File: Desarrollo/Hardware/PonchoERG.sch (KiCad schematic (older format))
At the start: 1 part

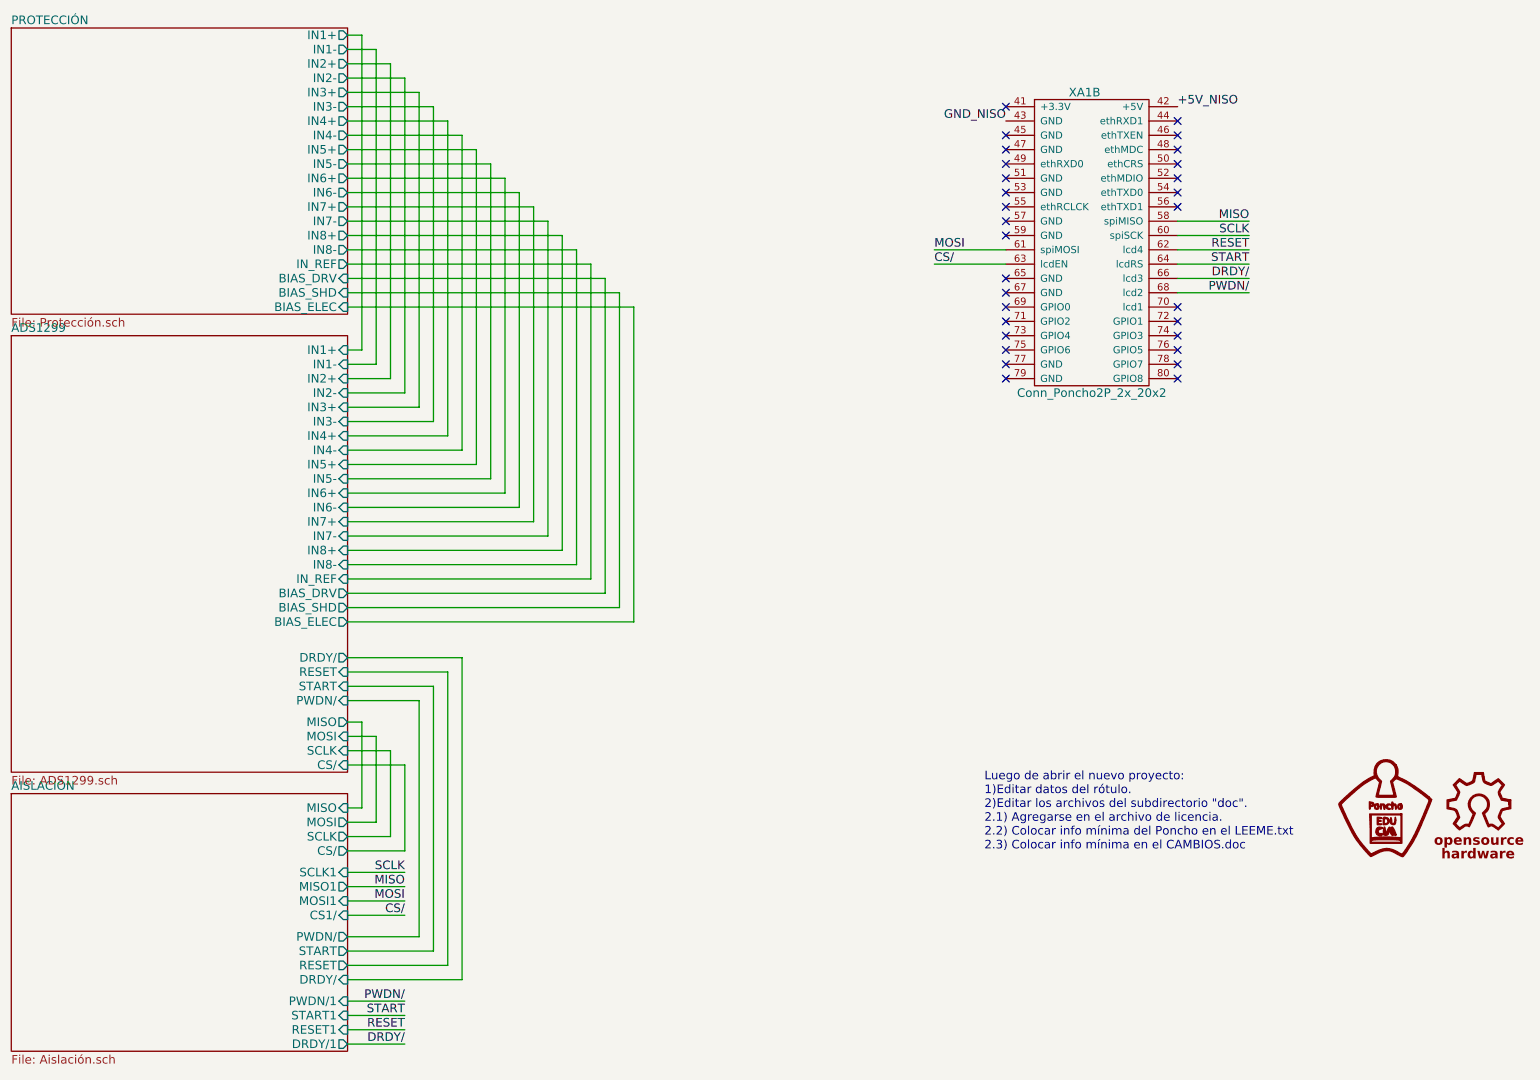
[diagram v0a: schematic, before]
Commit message: Revert "Finalización de primer ruteo estimado. Revisión de cantidad de v"
This reverts commit b379d941abb4cafe5355ba8bbe61a2a3831aeef6.
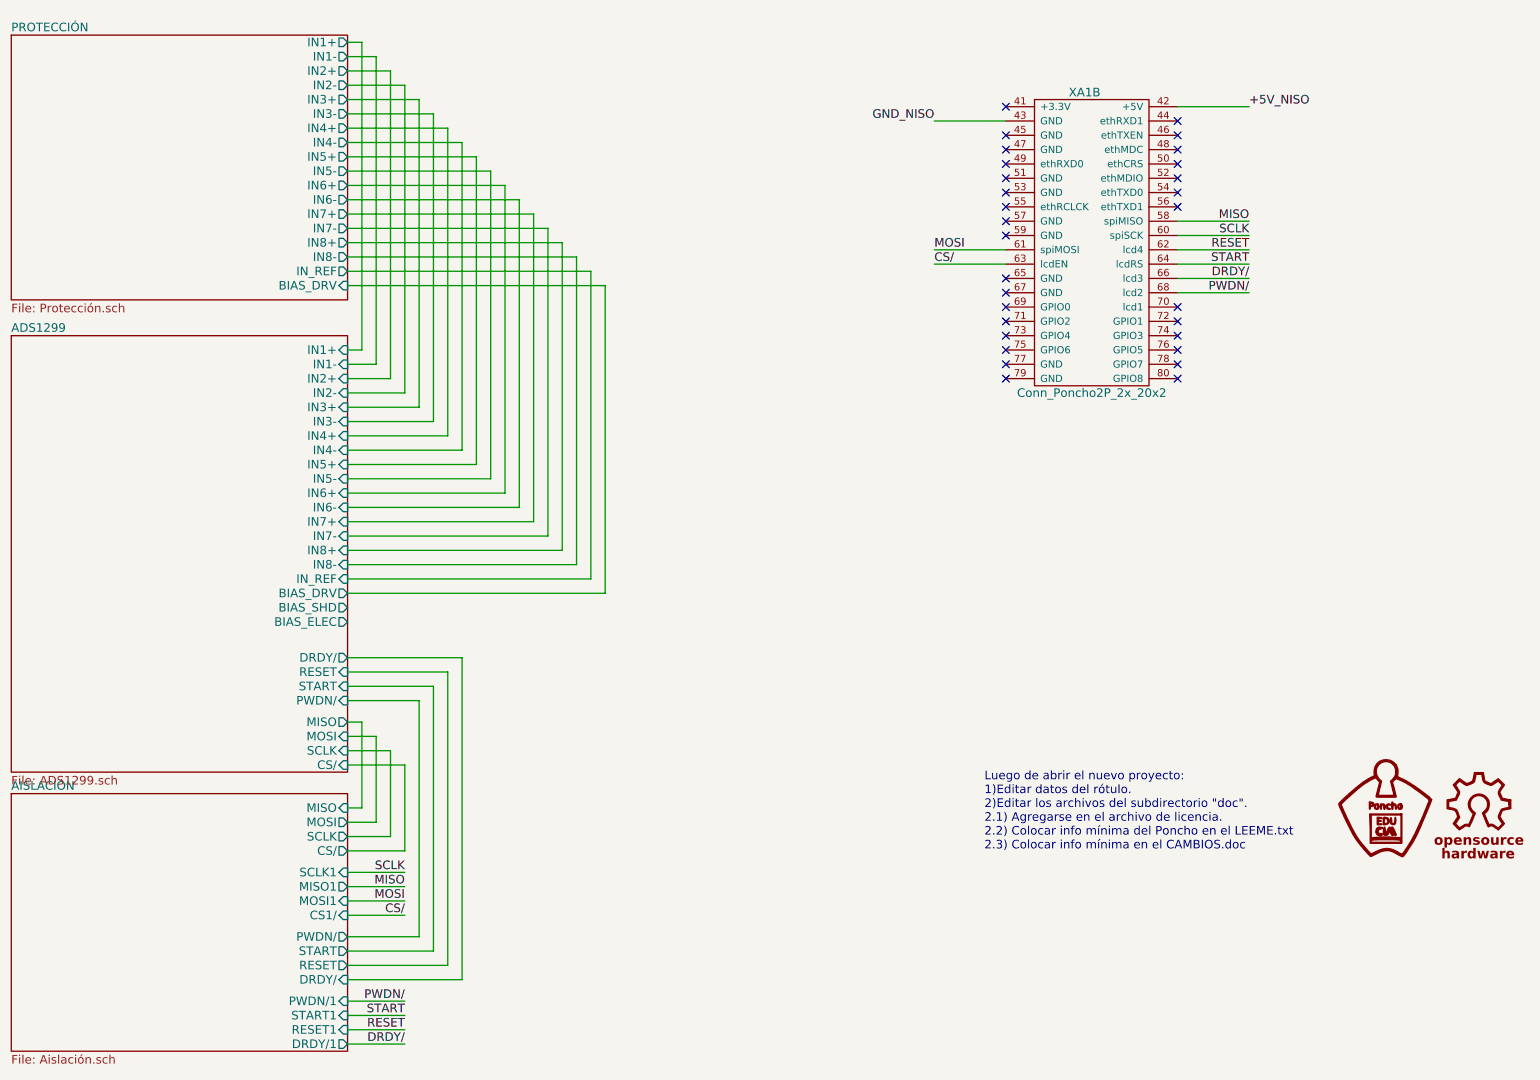
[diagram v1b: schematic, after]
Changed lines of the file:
@@
 Date "lun 05 oct 2015"
 Rev "1.0"
-Comp "Bruno Javier Cesario"
+Comp "Proyecto CIAA - COMPUTADORA INDUSTRIAL ABIERTA ARGENTINA"
 Comment1 "https://github.com/ciaa/Ponchos/tree/master/modelos/doc"
 Comment2 "Autores y Licencia del template (Diego Brengi - UNLaM)"
@@
 Luego de abrir el nuevo proyecto:\n1)Editar datos del rótulo.\n2)Editar los archivos del subdirectorio "doc".\n2.1) Agregarse en el archivo de licencia.\n2.2) Colocar info mínima del Poncho en el LEEME.txt\n2.3) Colocar info mínima en el CAMBIOS.doc
 $Sheet
-S 550  550  2350 2000
+S 550  600  2350 1850
 U 57BDBDC8
 F0 "PROTECCIÓN" 60
 F1 "Protección.sch" 60
-F2 "IN2-" O R 2900 900 60
-F3 "IN3+" O R 2900 1000 60
-F4 "IN3-" O R 2900 1100 60
-F5 "IN4+" O R 2900 1200 60
-F6 "IN4-" O R 2900 1300 60
-F7 "IN5+" O R 2900 1400 60
-F8 "IN5-" O R 2900 1500 60
-F9 "IN6+" O R 2900 1600 60
-F10 "IN6-" O R 2900 1700 60
-F11 "IN7+" O R 2900 1800 60
-F12 "IN1+" O R 2900 600 60
-F13 "IN1-" O R 2900 700 60
-F14 "IN2+" O R 2900 800 60
-F15 "IN7-" O R 2900 1900 60
-F16 "IN8+" O R 2900 2000 60
-F17 "IN8-" O R 2900 2100 60
-F18 "IN_REF" O R 2900 2200 60
-F19 "BIAS_DRV" I R 2900 2300 60
-F20 "BIAS_SHD" I R 2900 2400 60
-F21 "BIAS_ELEC" I R 2900 2500 60
+F2 "IN2-" O R 2900 950 60
+F3 "IN3+" O R 2900 1050 60
+F4 "IN3-" O R 2900 1150 60
+F5 "IN4+" O R 2900 1250 60
+F6 "IN4-" O R 2900 1350 60
+F7 "IN5+" O R 2900 1450 60
+F8 "IN5-" O R 2900 1550 60
+F9 "IN6+" O R 2900 1650 60
+F10 "IN6-" O R 2900 1750 60
+F11 "IN7+" O R 2900 1850 60
+F12 "IN1+" O R 2900 650 60
+F13 "IN1-" O R 2900 750 60
+F14 "IN2+" O R 2900 850 60
+F15 "IN7-" O R 2900 1950 60
+F16 "IN8+" O R 2900 2050 60
+F17 "IN8-" O R 2900 2150 60
+F18 "IN_REF" O R 2900 2250 60
+F19 "BIAS_DRV" I R 2900 2350 60
 $EndSheet
 $Sheet
@@
 $EndSheet
 Wire Wire Line
-	3000 600  3000 2800
+	2900 650  3000 650
+Wire Wire Line
+	3000 650  3000 2800
 Wire Wire Line
 	3000 2800 2900 2800
 Wire Wire Line
-	3100 700  3100 2900
+	2900 750  3100 750
+Wire Wire Line
+	3100 750  3100 2900
 Wire Wire Line
 	3100 2900 2900 2900
 Wire Wire Line
-	3200 3000 2900 3000
-Wire Wire Line
-	3200 800  3200 3000
-Wire Wire Line
-	3300 900  3300 3100
+	2900 3000 3200 3000
+Wire Wire Line
+	3200 3000 3200 850
+Wire Wire Line
+	3200 850  2900 850
+Wire Wire Line
+	2900 950  3300 950
+Wire Wire Line
+	3300 950  3300 3100
 Wire Wire Line
 	3300 3100 2900 3100
 Wire Wire Line
-	3400 1000 3400 3200
+	2900 1050 3400 1050
+Wire Wire Line
+	3400 1050 3400 3200
 Wire Wire Line
 	3400 3200 2900 3200
 Wire Wire Line
-	3500 1100 3500 3300
+	2900 1150 3500 1150
+Wire Wire Line
+	3500 1150 3500 3300
 Wire Wire Line
 	3500 3300 2900 3300
 Wire Wire Line
-	3600 3400 2900 3400
-Wire Wire Line
-	3600 1200 3600 3400
-Wire Wire Line
-	3700 1300 3700 3500
+	2900 3400 3600 3400
+Wire Wire Line
+	3600 3400 3600 1250
+Wire Wire Line
+	3600 1250 2900 1250
+Wire Wire Line
+	2900 1350 3700 1350
+Wire Wire Line
+	3700 1350 3700 3500
 Wire Wire Line
 	3700 3500 2900 3500
 Wire Wire Line
-	3800 3600 2900 3600
-Wire Wire Line
-	3800 1400 3800 3600
-Wire Wire Line
-	3900 1500 3900 3700
+	2900 3600 3800 3600
+Wire Wire Line
+	3800 3600 3800 1450
+Wire Wire Line
+	3800 1450 2900 1450
+Wire Wire Line
+	2900 1550 3900 1550
+Wire Wire Line
+	3900 1550 3900 3700
 Wire Wire Line
 	3900 3700 2900 3700
 Wire Wire Line
-	4000 3800 2900 3800
-Wire Wire Line
-	4000 1600 4000 3800
-Wire Wire Line
-	4100 1700 4100 3900
+	2900 3800 4000 3800
+Wire Wire Line
+	4000 3800 4000 1650
+Wire Wire Line
+	4000 1650 2900 1650
+Wire Wire Line
+	2900 1750 4100 1750
+Wire Wire Line
+	4100 1750 4100 3900
 Wire Wire Line
 	4100 3900 2900 3900
 Wire Wire Line
-	4200 1800 4200 4000
+	2900 1850 4200 1850
+Wire Wire Line
+	4200 1850 4200 4000
 Wire Wire Line
 	4200 4000 2900 4000
 Wire Wire Line
-	4300 1900 4300 4100
+	2900 1950 4300 1950
+Wire Wire Line
+	4300 1950 4300 4100
 Wire Wire Line
 	4300 4100 2900 4100
 Wire Wire Line
-	4400 4200 2900 4200
-Wire Wire Line
-	4400 2000 4400 4200
-Wire Wire Line
-	4500 4300 2900 4300
-Wire Wire Line
-	4500 2100 4500 4300
+	2900 4200 4400 4200
+Wire Wire Line
+	4400 4200 4400 2050
+Wire Wire Line
+	4400 2050 2900 2050
+Wire Wire Line
+	2900 4300 4500 4300
+Wire Wire Line
+	4500 4300 4500 2150
+Wire Wire Line
+	4500 2150 2900 2150
 Wire Wire Line
 	3000 6000 2900 6000
@@
 	2900 6300 3300 6300
 Wire Wire Line
-	4700 2300 4700 4500
+	2900 2350 4700 2350
+Wire Wire Line
+	4700 2350 4700 4500
 Wire Wire Line
 	4700 4500 2900 4500
 Wire Wire Line
-	4600 2200 4600 4400
+	2900 2250 4600 2250
+Wire Wire Line
+	4600 2250 4600 4400
 Wire Wire Line
 	4600 4400 2900 4400
@@
 	1    0    0    -1
 $EndComp
-Text Label 8700 1100 0    60   ~ 0
+Wire Wire Line
+	8700 1100 9200 1100
+Wire Wire Line
+	7500 1200 7000 1200
+Text Label 9200 1100 0    60   ~ 0
 +5V_NISO
-Text Label 7500 1200 2    60   ~ 0
+Text Label 7000 1200 2    60   ~ 0
 GND_NISO
 Wire Wire Line
@@
 Wire Wire Line
 	3700 4950 2900 4950
-Wire Wire Line
-	2900 600  3000 600
-Wire Wire Line
-	2900 700  3100 700
-Wire Wire Line
-	2900 800  3200 800
-Wire Wire Line
-	2900 900  3300 900
-Wire Wire Line
-	2900 1000 3400 1000
-Wire Wire Line
-	2900 1100 3500 1100
-Wire Wire Line
-	2900 1200 3600 1200
-Wire Wire Line
-	2900 1300 3700 1300
-Wire Wire Line
-	2900 1400 3800 1400
-Wire Wire Line
-	2900 1500 3900 1500
-Wire Wire Line
-	2900 1600 4000 1600
-Wire Wire Line
-	4100 1700 2900 1700
-Wire Wire Line
-	2900 1800 4200 1800
-Wire Wire Line
-	2900 1900 4300 1900
-Wire Wire Line
-	2900 2000 4400 2000
-Wire Wire Line
-	2900 2100 4500 2100
-Wire Wire Line
-	2900 2200 4600 2200
-Wire Wire Line
-	2900 2300 4700 2300
-Wire Wire Line
-	2900 4600 4800 4600
-Wire Wire Line
-	4800 4600 4800 2400
-Wire Wire Line
-	4800 2400 2900 2400
-Wire Wire Line
-	2900 2500 4900 2500
-Wire Wire Line
-	4900 2500 4900 4700
-Wire Wire Line
-	4900 4700 2900 4700
 $EndSCHEMATC

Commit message: Finalización de primer ruteo estimado. Revisión de cantidad de v
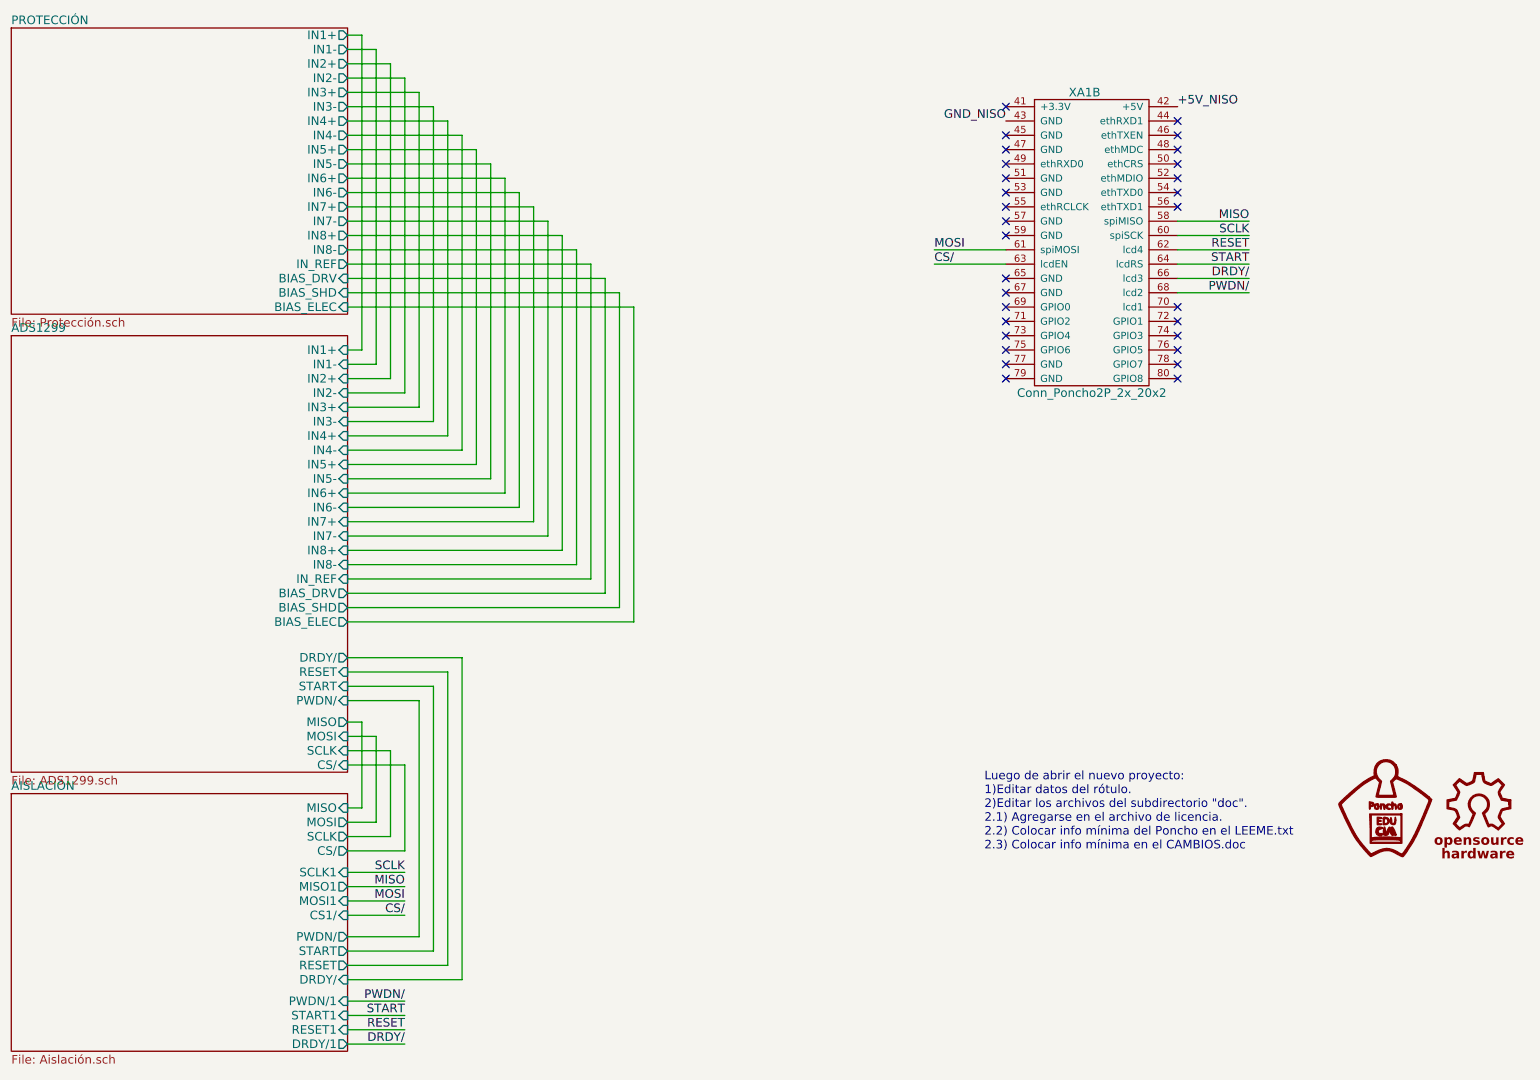
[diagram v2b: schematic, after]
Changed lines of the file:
@@
 Date "lun 05 oct 2015"
 Rev "1.0"
-Comp "Proyecto CIAA - COMPUTADORA INDUSTRIAL ABIERTA ARGENTINA"
+Comp "Bruno Javier Cesario"
 Comment1 "https://github.com/ciaa/Ponchos/tree/master/modelos/doc"
 Comment2 "Autores y Licencia del template (Diego Brengi - UNLaM)"
@@
 Luego de abrir el nuevo proyecto:\n1)Editar datos del rótulo.\n2)Editar los archivos del subdirectorio "doc".\n2.1) Agregarse en el archivo de licencia.\n2.2) Colocar info mínima del Poncho en el LEEME.txt\n2.3) Colocar info mínima en el CAMBIOS.doc
 $Sheet
-S 550  600  2350 1850
+S 550  550  2350 2000
 U 57BDBDC8
 F0 "PROTECCIÓN" 60
 F1 "Protección.sch" 60
-F2 "IN2-" O R 2900 950 60
-F3 "IN3+" O R 2900 1050 60
-F4 "IN3-" O R 2900 1150 60
-F5 "IN4+" O R 2900 1250 60
-F6 "IN4-" O R 2900 1350 60
-F7 "IN5+" O R 2900 1450 60
-F8 "IN5-" O R 2900 1550 60
-F9 "IN6+" O R 2900 1650 60
-F10 "IN6-" O R 2900 1750 60
-F11 "IN7+" O R 2900 1850 60
-F12 "IN1+" O R 2900 650 60
-F13 "IN1-" O R 2900 750 60
-F14 "IN2+" O R 2900 850 60
-F15 "IN7-" O R 2900 1950 60
-F16 "IN8+" O R 2900 2050 60
-F17 "IN8-" O R 2900 2150 60
-F18 "IN_REF" O R 2900 2250 60
-F19 "BIAS_DRV" I R 2900 2350 60
+F2 "IN2-" O R 2900 900 60
+F3 "IN3+" O R 2900 1000 60
+F4 "IN3-" O R 2900 1100 60
+F5 "IN4+" O R 2900 1200 60
+F6 "IN4-" O R 2900 1300 60
+F7 "IN5+" O R 2900 1400 60
+F8 "IN5-" O R 2900 1500 60
+F9 "IN6+" O R 2900 1600 60
+F10 "IN6-" O R 2900 1700 60
+F11 "IN7+" O R 2900 1800 60
+F12 "IN1+" O R 2900 600 60
+F13 "IN1-" O R 2900 700 60
+F14 "IN2+" O R 2900 800 60
+F15 "IN7-" O R 2900 1900 60
+F16 "IN8+" O R 2900 2000 60
+F17 "IN8-" O R 2900 2100 60
+F18 "IN_REF" O R 2900 2200 60
+F19 "BIAS_DRV" I R 2900 2300 60
+F20 "BIAS_SHD" I R 2900 2400 60
+F21 "BIAS_ELEC" I R 2900 2500 60
 $EndSheet
 $Sheet
@@
 $EndSheet
 Wire Wire Line
-	2900 650  3000 650
-Wire Wire Line
-	3000 650  3000 2800
+	3000 600  3000 2800
 Wire Wire Line
 	3000 2800 2900 2800
 Wire Wire Line
-	2900 750  3100 750
-Wire Wire Line
-	3100 750  3100 2900
+	3100 700  3100 2900
 Wire Wire Line
 	3100 2900 2900 2900
 Wire Wire Line
-	2900 3000 3200 3000
-Wire Wire Line
-	3200 3000 3200 850
-Wire Wire Line
-	3200 850  2900 850
-Wire Wire Line
-	2900 950  3300 950
-Wire Wire Line
-	3300 950  3300 3100
+	3200 3000 2900 3000
+Wire Wire Line
+	3200 800  3200 3000
+Wire Wire Line
+	3300 900  3300 3100
 Wire Wire Line
 	3300 3100 2900 3100
 Wire Wire Line
-	2900 1050 3400 1050
-Wire Wire Line
-	3400 1050 3400 3200
+	3400 1000 3400 3200
 Wire Wire Line
 	3400 3200 2900 3200
 Wire Wire Line
-	2900 1150 3500 1150
-Wire Wire Line
-	3500 1150 3500 3300
+	3500 1100 3500 3300
 Wire Wire Line
 	3500 3300 2900 3300
 Wire Wire Line
-	2900 3400 3600 3400
-Wire Wire Line
-	3600 3400 3600 1250
-Wire Wire Line
-	3600 1250 2900 1250
-Wire Wire Line
-	2900 1350 3700 1350
-Wire Wire Line
-	3700 1350 3700 3500
+	3600 3400 2900 3400
+Wire Wire Line
+	3600 1200 3600 3400
+Wire Wire Line
+	3700 1300 3700 3500
 Wire Wire Line
 	3700 3500 2900 3500
 Wire Wire Line
-	2900 3600 3800 3600
-Wire Wire Line
-	3800 3600 3800 1450
-Wire Wire Line
-	3800 1450 2900 1450
-Wire Wire Line
-	2900 1550 3900 1550
-Wire Wire Line
-	3900 1550 3900 3700
+	3800 3600 2900 3600
+Wire Wire Line
+	3800 1400 3800 3600
+Wire Wire Line
+	3900 1500 3900 3700
 Wire Wire Line
 	3900 3700 2900 3700
 Wire Wire Line
-	2900 3800 4000 3800
-Wire Wire Line
-	4000 3800 4000 1650
-Wire Wire Line
-	4000 1650 2900 1650
-Wire Wire Line
-	2900 1750 4100 1750
-Wire Wire Line
-	4100 1750 4100 3900
+	4000 3800 2900 3800
+Wire Wire Line
+	4000 1600 4000 3800
+Wire Wire Line
+	4100 1700 4100 3900
 Wire Wire Line
 	4100 3900 2900 3900
 Wire Wire Line
-	2900 1850 4200 1850
-Wire Wire Line
-	4200 1850 4200 4000
+	4200 1800 4200 4000
 Wire Wire Line
 	4200 4000 2900 4000
 Wire Wire Line
-	2900 1950 4300 1950
-Wire Wire Line
-	4300 1950 4300 4100
+	4300 1900 4300 4100
 Wire Wire Line
 	4300 4100 2900 4100
 Wire Wire Line
-	2900 4200 4400 4200
-Wire Wire Line
-	4400 4200 4400 2050
-Wire Wire Line
-	4400 2050 2900 2050
-Wire Wire Line
-	2900 4300 4500 4300
-Wire Wire Line
-	4500 4300 4500 2150
-Wire Wire Line
-	4500 2150 2900 2150
+	4400 4200 2900 4200
+Wire Wire Line
+	4400 2000 4400 4200
+Wire Wire Line
+	4500 4300 2900 4300
+Wire Wire Line
+	4500 2100 4500 4300
 Wire Wire Line
 	3000 6000 2900 6000
@@
 	2900 6300 3300 6300
 Wire Wire Line
-	2900 2350 4700 2350
-Wire Wire Line
-	4700 2350 4700 4500
+	4700 2300 4700 4500
 Wire Wire Line
 	4700 4500 2900 4500
 Wire Wire Line
-	2900 2250 4600 2250
-Wire Wire Line
-	4600 2250 4600 4400
+	4600 2200 4600 4400
 Wire Wire Line
 	4600 4400 2900 4400
@@
 	1    0    0    -1
 $EndComp
-Wire Wire Line
-	8700 1100 9200 1100
-Wire Wire Line
-	7500 1200 7000 1200
-Text Label 9200 1100 0    60   ~ 0
+Text Label 8700 1100 0    60   ~ 0
 +5V_NISO
-Text Label 7000 1200 2    60   ~ 0
+Text Label 7500 1200 2    60   ~ 0
 GND_NISO
 Wire Wire Line
@@
 Wire Wire Line
 	3700 4950 2900 4950
+Wire Wire Line
+	2900 600  3000 600
+Wire Wire Line
+	2900 700  3100 700
+Wire Wire Line
+	2900 800  3200 800
+Wire Wire Line
+	2900 900  3300 900
+Wire Wire Line
+	2900 1000 3400 1000
+Wire Wire Line
+	2900 1100 3500 1100
+Wire Wire Line
+	2900 1200 3600 1200
+Wire Wire Line
+	2900 1300 3700 1300
+Wire Wire Line
+	2900 1400 3800 1400
+Wire Wire Line
+	2900 1500 3900 1500
+Wire Wire Line
+	2900 1600 4000 1600
+Wire Wire Line
+	4100 1700 2900 1700
+Wire Wire Line
+	2900 1800 4200 1800
+Wire Wire Line
+	2900 1900 4300 1900
+Wire Wire Line
+	2900 2000 4400 2000
+Wire Wire Line
+	2900 2100 4500 2100
+Wire Wire Line
+	2900 2200 4600 2200
+Wire Wire Line
+	2900 2300 4700 2300
+Wire Wire Line
+	2900 4600 4800 4600
+Wire Wire Line
+	4800 4600 4800 2400
+Wire Wire Line
+	4800 2400 2900 2400
+Wire Wire Line
+	2900 2500 4900 2500
+Wire Wire Line
+	4900 2500 4900 4700
+Wire Wire Line
+	4900 4700 2900 4700
 $EndSCHEMATC
